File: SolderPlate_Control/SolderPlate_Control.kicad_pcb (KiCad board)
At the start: 2 copper layers, 29 x 29 mm, 23 parts, among them J1 Encoder, J2 Conn_01x04, Q1 Si2301CDS, Q3 BSS138, Q4 Si2301CDS, U1 PEL12D

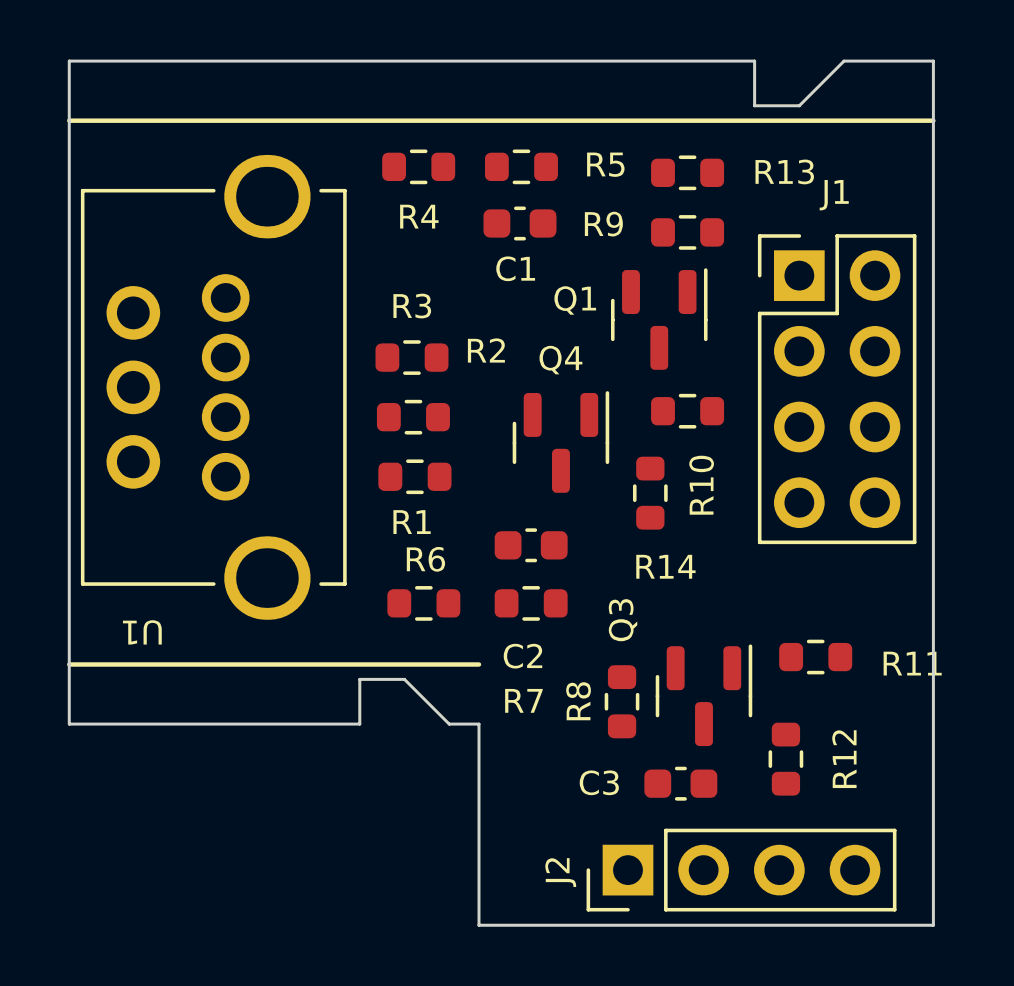
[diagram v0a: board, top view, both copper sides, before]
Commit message: Reduced Encoder control circuit to fit
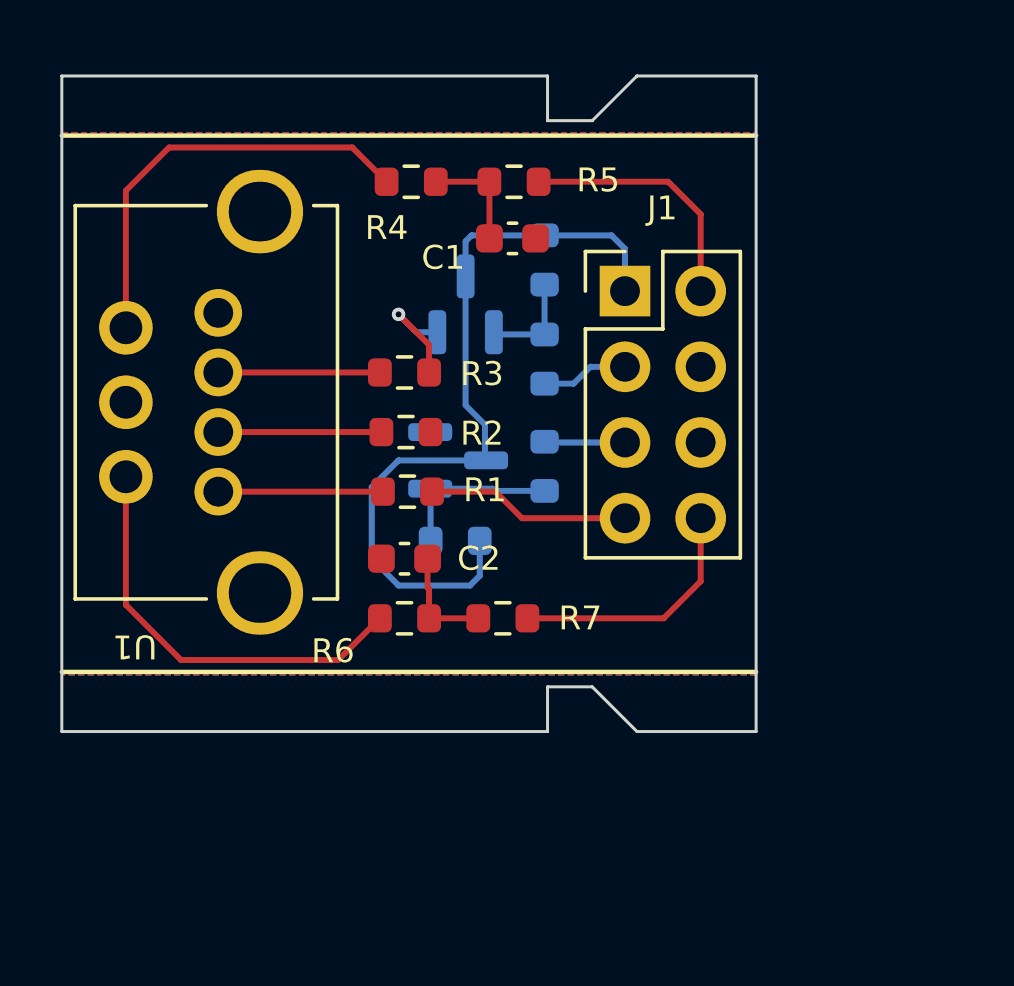
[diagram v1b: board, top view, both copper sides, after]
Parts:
- removed C3: 100nF, Capacitor_SMD:C_0603_1608Metric
- removed J2: Conn_01x04, Connector_PinHeader_2.54mm:PinHeader_1x04_P2.54mm_Vertical
- removed Q3: BSS138, Package_TO_SOT_SMD:SOT-23
- removed R11: 470, Resistor_SMD:R_0603_1608Metric
- removed R12: 68, Resistor_SMD:R_0603_1608Metric
- removed R8: 10K, Resistor_SMD:R_0603_1608Metric
- Q1, Q4, R10, R13, R14, R9: moved to B.Cu
- moved R14 6.74 mm to (82.2, 58.6), turned to 0 degrees
- moved Q1 6.52 mm to (82.5, 50.7), turned to 90 degrees
- moved R9 6.41 mm to (85.2, 52.5), turned to 90 degrees
- moved J1 5.87 mm to (87.9, 50.2)
- moved R13 5.62 mm to (85.2, 49.2), turned to 90 degrees
- moved R10 5.14 mm to (85.2, 56.1), turned to -90 degrees
- moved C2 4.27 mm to (80.5, 59.2), turned to 180 degrees
- moved Q4 3.50 mm to (82.3, 55.9), turned to 0 degrees
- moved R7 1.07 mm to (83.8, 61.2)
- moved R6 0.82 mm to (80.5, 61.2)
- moved C1 0.56 mm to (84.1, 48.5)
- moved R1 0.56 mm to (80.6, 57.0)
- moved R2 0.56 mm to (80.5, 55.0)
- moved R3 0.56 mm to (80.5, 53.0)
- moved R4 0.56 mm to (80.7, 46.5)
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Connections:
- J1 pad 6: /Contrast -> unconnected-(J1-Pin_6-Pad6)
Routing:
- net +5V: track 0.00 -> 26.6 mm
- net Net-(U1-A): track 0.00 -> 14.4 mm
- net Net-(U1-B): track 0.00 -> 14.2 mm
- net /Enc_A: track 0.00 -> 8.47 mm
- net /Enc_B: track 0.00 -> 8.45 mm
- net /Enc_SW: track 0.00 -> 6.84 mm
- net Net-(Q4-G): track 0.00 -> 5.62 mm
- net Net-(U1-SW): track 0.00 -> 5.53 mm
- net Net-(U1-A2): track 0.00 -> 5.47 mm
- net Net-(U1-A1): track 0.00 -> 5.42 mm
- net Net-(Q1-S): track 0.00 -> 4.29 mm, vias 0 -> 1
- net Net-(C1-Pad1): track 0.00 -> 3.70 mm
- net Net-(C2-Pad1): track 0.00 -> 3.67 mm
- net Net-(Q1-G): track 0.00 -> 3.41 mm
- net /LED_Blue: track 0.00 -> 2.93 mm
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- added copper zone on B.Cu, net GND
- added copper zone on F.Cu, net GND
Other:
- board size 29 x 29 mm -> 23.3 x 22 mm

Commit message: Final PCBs and production files. Added latch for control wheel circuit
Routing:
- net Net-(Q4-S): track 0.00 -> 1.93 mm, vias 0 -> 1
- net GND: vias 0 -> 41
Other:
- board text added: "JLCJLCJLCJLC"
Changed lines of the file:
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@@
     )
     (pad_to_mask_clearance 0)
+    (aux_axis_origin 69 65)
+    (grid_origin 69 65)
     (pcbplotparams
       (layerselection 0x00010fc_ffffffff)
@@
     )
   )
-  (gr_line (start 69 45) (end 92.3 45)
+  (gr_line (start 69.2 45) (end 92 45)
     (stroke (width 0.15) (type default)) (layer "F.SilkS"))
-  (gr_line (start 69 63) (end 92.3 63)
+  (gr_line (start 69.2 63) (end 92 63)
     (stroke (width 0.15) (type default)) (layer "F.SilkS"))
   (gr_line (start 88.3 43) (end 86.8 44.5)
@@
   (gr_line (start 69 65) (end 85.3 65)
     (stroke (width 0.1) (type default)) (layer "Edge.Cuts"))
-  (dimension (type aligned) (layer "F.SilkS")
+  (gr_text "JLCJLCJLCJLC" (at 69.5 64.5) (layer "F.SilkS")
+    (effects (font (size 0.9 0.9) (thickness 0.15)) (justify left bottom))
+  )
+  (dimension (type aligned) (layer "Cmts.User")
+    (pts (xy 92.3 65) (xy 92.3 43))
+    (height 3.9)
+    (gr_text "22.0000 mm" (at 95.05 54 90) (layer "Cmts.User")
+      (effects (font (size 1 1) (thickness 0.15)))
+    )
+    (format (prefix "") (suffix "") (units 3) (units_format 1) (precision 4))
+    (style (thickness 0.15) (arrow_length 1.27) (text_position_mode 0) (extension_height 0.58642) (extension_offset 0.5) keep_text_aligned)
+  )
+  (dimension (type aligned) (layer "Cmts.User")
     (pts (xy 92.3 43) (xy 69 43))
     (height 3)
-    (gr_text "23.3000 mm" (at 80.65 38.85) (layer "F.SilkS")
+    (gr_text "23.3000 mm" (at 80.65 38.85) (layer "Cmts.User")
       (effects (font (size 1 1) (thickness 0.15)))
     )
@@
     (style (thickness 0.15) (arrow_length 1.27) (text_position_mode 0) (extension_height 0.58642) (extension_offset 0.5) keep_text_aligned)
   )
+  (dimension (type aligned) (layer "Cmts.User")
+    (pts (xy 69 43) (xy 85.3 43))
+    (height -1)
+    (gr_text "16.3000 mm" (at 77.15 40.85) (layer "Cmts.User")
+      (effects (font (size 1 1) (thickness 0.15)))
+    )
+    (format (prefix "") (suffix "") (units 3) (units_format 1) (precision 4))
+    (style (thickness 0.15) (arrow_length 1.27) (text_position_mode 0) (extension_height 0.58642) (extension_offset 0.5) keep_text_aligned)
+  )
   (segment (start 83.35 46.55) (end 83.35 48.45) (width 0.2) (layer "F.Cu") (net 1))
   (segment (start 83.35 46.55) (end 81.55 46.55) (width 0.2) (layer "F.Cu") (net 1))
+  (via (at 70.2 59) (size 0.45) (drill 0.2) (layers "F.Cu" "B.Cu") (free) (net 2))
+  (via (at 73 46.4) (size 0.45) (drill 0.2) (layers "F.Cu" "B.Cu") (free) (net 2))
+  (via (at 80 62.4) (size 0.45) (drill 0.2) (layers "F.Cu" "B.Cu") (free) (net 2))
+  (via (at 86.2 47.4) (size 0.45) (drill 0.2) (layers "F.Cu" "B.Cu") (free) (net 2))
+  (via (at 89 62) (size 0.45) (drill 0.2) (layers "F.Cu" "B.Cu") (free) (net 2))
+  (via (at 79 51.6) (size 0.45) (drill 0.2) (layers "F.Cu" "B.Cu") (free) (net 2))
+  (via (at 86 45.6) (size 0.45) (drill 0.2) (layers "F.Cu" "B.Cu") (free) (net 2))
+  (via (at 76 56) (size 0.45) (drill 0.2) (layers "F.Cu" "B.Cu") (free) (net 2))
+  (via (at 84.2 60) (size 0.45) (drill 0.2) (layers "F.Cu" "B.Cu") (free) (net 2))
+  (via (at 86.6 56.6) (size 0.45) (drill 0.2) (layers "F.Cu" "B.Cu") (free) (net 2))
+  (via (at 89.2 56.6) (size 0.45) (drill 0.2) (layers "F.Cu" "B.Cu") (free) (net 2))
+  (via (at 76 54) (size 0.45) (drill 0.2) (layers "F.Cu" "B.Cu") (free) (net 2))
+  (via (at 86.6 54.2) (size 0.45) (drill 0.2) (layers "F.Cu" "B.Cu") (free) (net 2))
+  (via (at 70.2 46.2) (size 0.45) (drill 0.2) (layers "F.Cu" "B.Cu") (free) (net 2))
+  (via (at 73.8 49.4) (size 0.45) (drill 0.2) (layers "F.Cu" "B.Cu") (free) (net 2))
+  (via (at 76 51.8) (size 0.45) (drill 0.2) (layers "F.Cu" "B.Cu") (free) (net 2))
+  (via (at 84.6 62.4) (size 0.45) (drill 0.2) (layers "F.Cu" "B.Cu") (free) (net 2))
+  (via (at 88.8 48.4) (size 0.45) (drill 0.2) (layers "F.Cu" "B.Cu") (free) (net 2))
+  (via (at 73.8 58.4) (size 0.45) (drill 0.2) (layers "F.Cu" "B.Cu") (free) (net 2))
+  (via (at 89.2 51.6) (size 0.45) (drill 0.2) (layers "F.Cu" "B.Cu") (free) (net 2))
+  (via (at 77.2 51.8) (size 0.45) (drill 0.2) (layers "F.Cu" "B.Cu") (free) (net 2))
+  (via (at 72.6 52.6) (size 0.45) (drill 0.2) (layers "F.Cu" "B.Cu") (free) (net 2))
+  (via (at 77.2 54) (size 0.45) (drill 0.2) (layers "F.Cu" "B.Cu") (free) (net 2))
+  (via (at 81.8 47.8) (size 0.45) (drill 0.2) (layers "F.Cu" "B.Cu") (free) (net 2))
+  (via (at 88.6 45.6) (size 0.45) (drill 0.2) (layers "F.Cu" "B.Cu") (free) (net 2))
+  (via (at 87 62) (size 0.45) (drill 0.2) (layers "F.Cu" "B.Cu") (free) (net 2))
+  (via (at 77.2 49.6) (size 0.45) (drill 0.2) (layers "F.Cu" "B.Cu") (free) (net 2))
+  (via (at 72.6 55.4) (size 0.45) (drill 0.2) (layers "F.Cu" "B.Cu") (free) (net 2))
+  (via (at 70.2 49) (size 0.45) (drill 0.2) (layers "F.Cu" "B.Cu") (free) (net 2))
+  (via (at 70.2 62) (size 0.45) (drill 0.2) (layers "F.Cu" "B.Cu") (free) (net 2))
+  (via (at 84.4 58.6) (size 0.45) (drill 0.2) (layers "F.Cu" "B.Cu") (free) (net 2))
+  (via (at 77.2 58.4) (size 0.45) (drill 0.2) (layers "F.Cu" "B.Cu") (free) (net 2))
+  (via (at 78.4 46.4) (size 0.45) (drill 0.2) (layers "F.Cu" "B.Cu") (free) (net 2))
+  (via (at 89.2 54) (size 0.45) (drill 0.2) (layers "F.Cu" "B.Cu") (free) (net 2))
+  (via (at 79.6 50.2) (size 0.45) (drill 0.2) (layers "F.Cu" "B.Cu") (free) (net 2))
+  (via (at 91 62) (size 0.45) (drill 0.2) (layers "F.Cu" "B.Cu") (free) (net 2))
+  (via (at 83.8 49.6) (size 0.45) (drill 0.2) (layers "F.Cu" "B.Cu") (free) (net 2))
+  (via (at 87.6 47.6) (size 0.45) (drill 0.2) (layers "F.Cu" "B.Cu") (free) (net 2))
+  (via (at 82 62.4) (size 0.45) (drill 0.2) (layers "F.Cu" "B.Cu") (free) (net 2))
+  (via (at 91 46) (size 0.45) (drill 0.2) (layers "F.Cu" "B.Cu") (free) (net 2))
+  (via (at 77.2 56) (size 0.45) (drill 0.2) (layers "F.Cu" "B.Cu") (free) (net 2))
   (segment (start 81.325 60.225) (end 81.325 61.2) (width 0.2) (layer "F.Cu") (net 3))
   (segment (start 82.975 61.2) (end 81.325 61.2) (width 0.2) (layer "F.Cu") (net 3))
@@
   (segment (start 87.9 55.3) (end 85.225 55.3) (width 0.2) (layer "B.Cu") (net 9))
   (segment (start 85.225 55.3) (end 85.2 55.275) (width 0.2) (layer "B.Cu") (net 9))
-  (segment (start 81.375 53) (end 81.325 52.95) (width 0.2) (layer "F.Cu") (net 10))
   (segment (start 81.325 52.025) (end 81.325 52.95) (width 0.2) (layer "F.Cu") (net 10))
   (segment (start 80.3 51) (end 81.325 52.025) (width 0.2) (layer "F.Cu") (net 10))
   (via (at 80.3 51) (size 0.45) (drill 0.2) (layers "F.Cu" "B.Cu") (net 10))
-  (segment (start 81.6 51.6) (end 81.6 51.9) (width 0.2) (layer "B.Cu") (net 10))
   (segment (start 81.6 51.6) (end 80.9 51.6) (width 0.2) (layer "B.Cu") (net 10))
   (segment (start 80.9 51.6) (end 80.3 51) (width 0.2) (layer "B.Cu") (net 10))
@@
   (segment (start 85.2 50) (end 85.2 51.675) (width 0.2) (layer "B.Cu") (net 18))
   (segment (start 85.2 51.675) (end 83.575 51.675) (width 0.2) (layer "B.Cu") (net 18))
+  (segment (start 81.375 54.025) (end 81.4 54) (width 0.25) (layer "F.Cu") (net 19))
+  (segment (start 81.375 54.95) (end 81.375 54.025) (width 0.25) (layer "F.Cu") (net 19))
+  (via (at 81.4 54) (size 0.45) (drill 0.2) (layers "F.Cu" "B.Cu") (net 19))
+  (segment (start 81.4 54) (end 81.4 54.9125) (width 0.25) (layer "B.Cu") (net 19))
+  (segment (start 81.4 54.9125) (end 81.3625 54.95) (width 0.25) (layer "B.Cu") (net 19))
   (zone (net 2) (net_name "GND") (layers "F&B.Cu") (hatch edge 0.5)
     (connect_pads yes (clearance 0.2))
